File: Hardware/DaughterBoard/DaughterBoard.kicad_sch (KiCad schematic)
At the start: 13 parts, among them J1 CARTDRIGE, J2 ROM, J3 ISA00, J4 ISA10, J7 ISA01, J8 ISA11, SW1 RESET

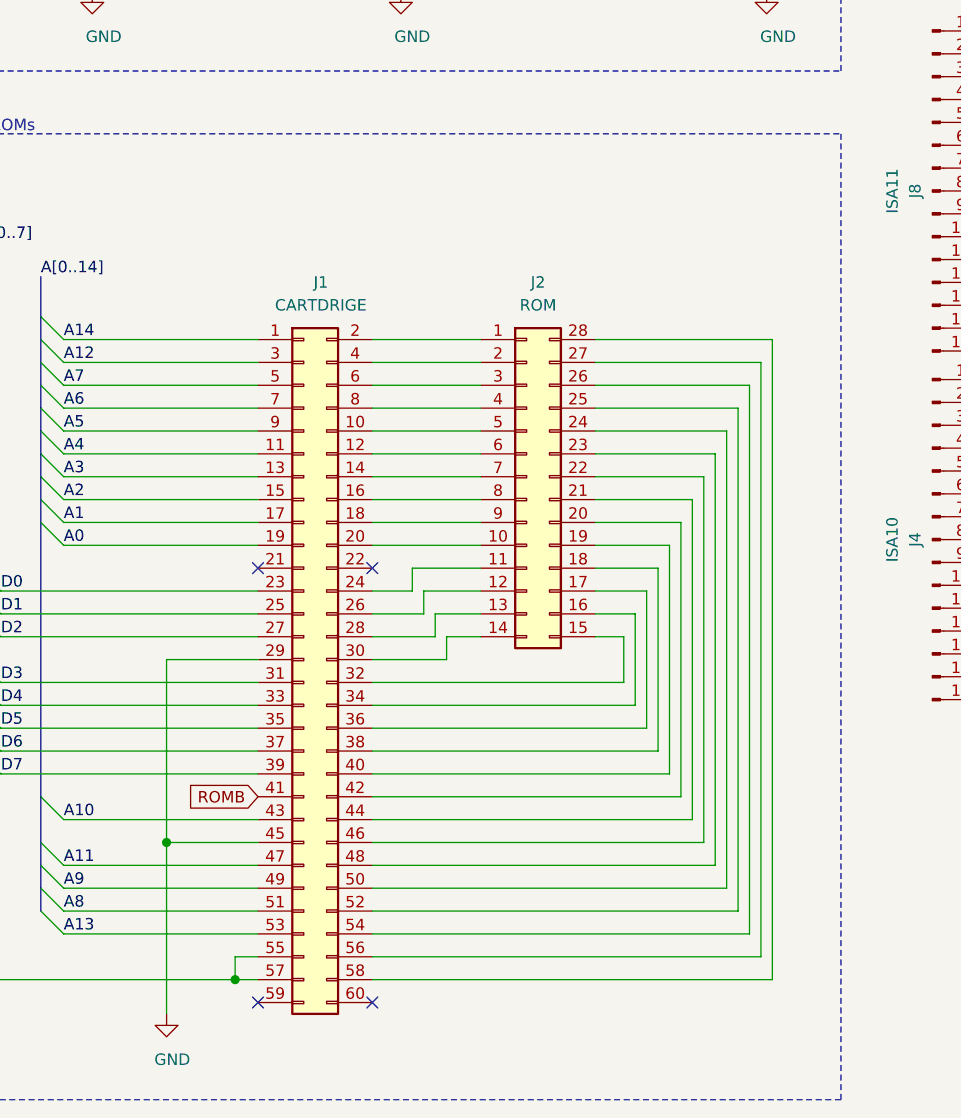
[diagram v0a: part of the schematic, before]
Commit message: implement graphic loading from ROM
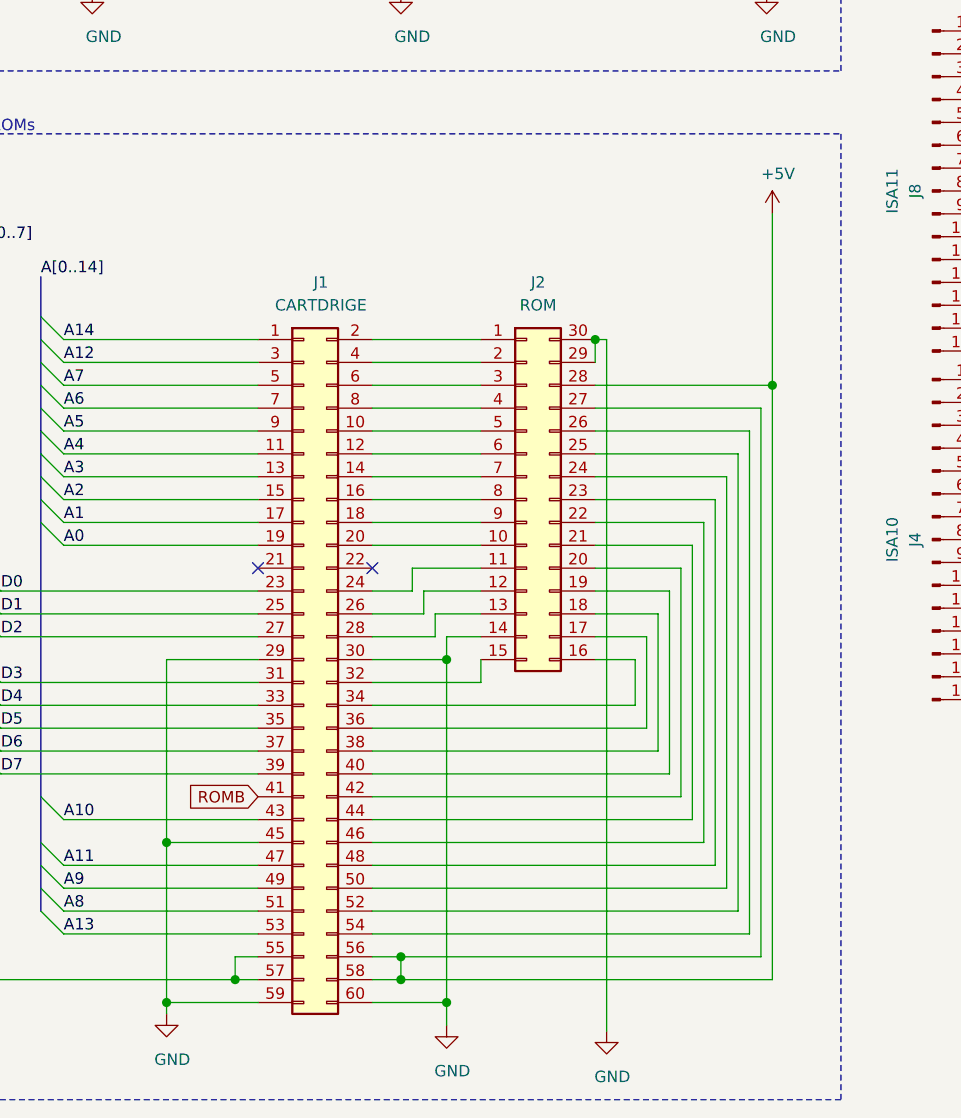
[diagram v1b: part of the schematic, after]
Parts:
- J1: footprint Connector_PCBEdge:Samtec_MECF-30-02-L-DV_2x30_P1.27mm_Polarized_Socket_Horizontal -> Connector_PCBEdge:Samtec_MECF-30-01-L-DV-WT_2x30_P1.27mm_Polarized_Socket_Horizontal
- J2: footprint Connector_PinHeader_2.54mm:PinHeader_2x14_P2.54mm_Vertical -> Connector_PinHeader_2.54mm:PinHeader_2x15_P2.54mm_Vertical; symbol Connector_Generic:Conn_02x14_Counter_Clockwise -> Connector_Generic:Conn_02x15_Counter_Clockwise
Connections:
- net +5V: now also J1.56 (Pin_56), J1.58 (Pin_58), J2.27 (Pin_27), J2.28 (Pin_28)
- net GND: now also J1.30 (Pin_30), J1.59 (Pin_59), J1.60 (Pin_60), J2.14 (Pin_14), J2.29 (Pin_29), J2.30 (Pin_30)
- no-connect marks 5 -> 3

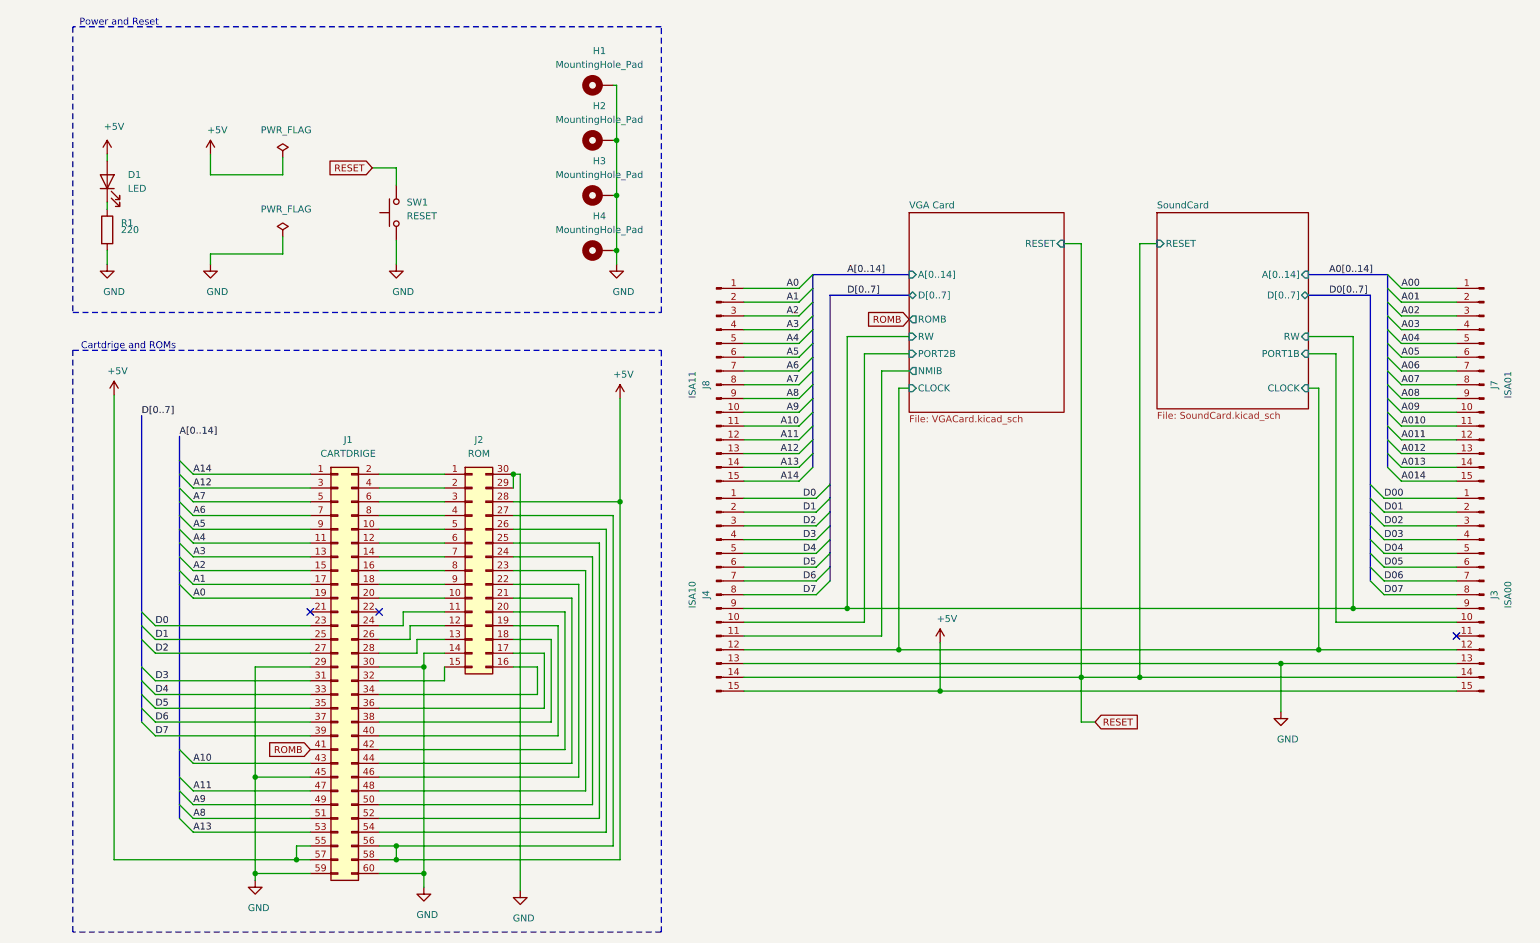
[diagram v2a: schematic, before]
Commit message: Implement APU and fix schematics
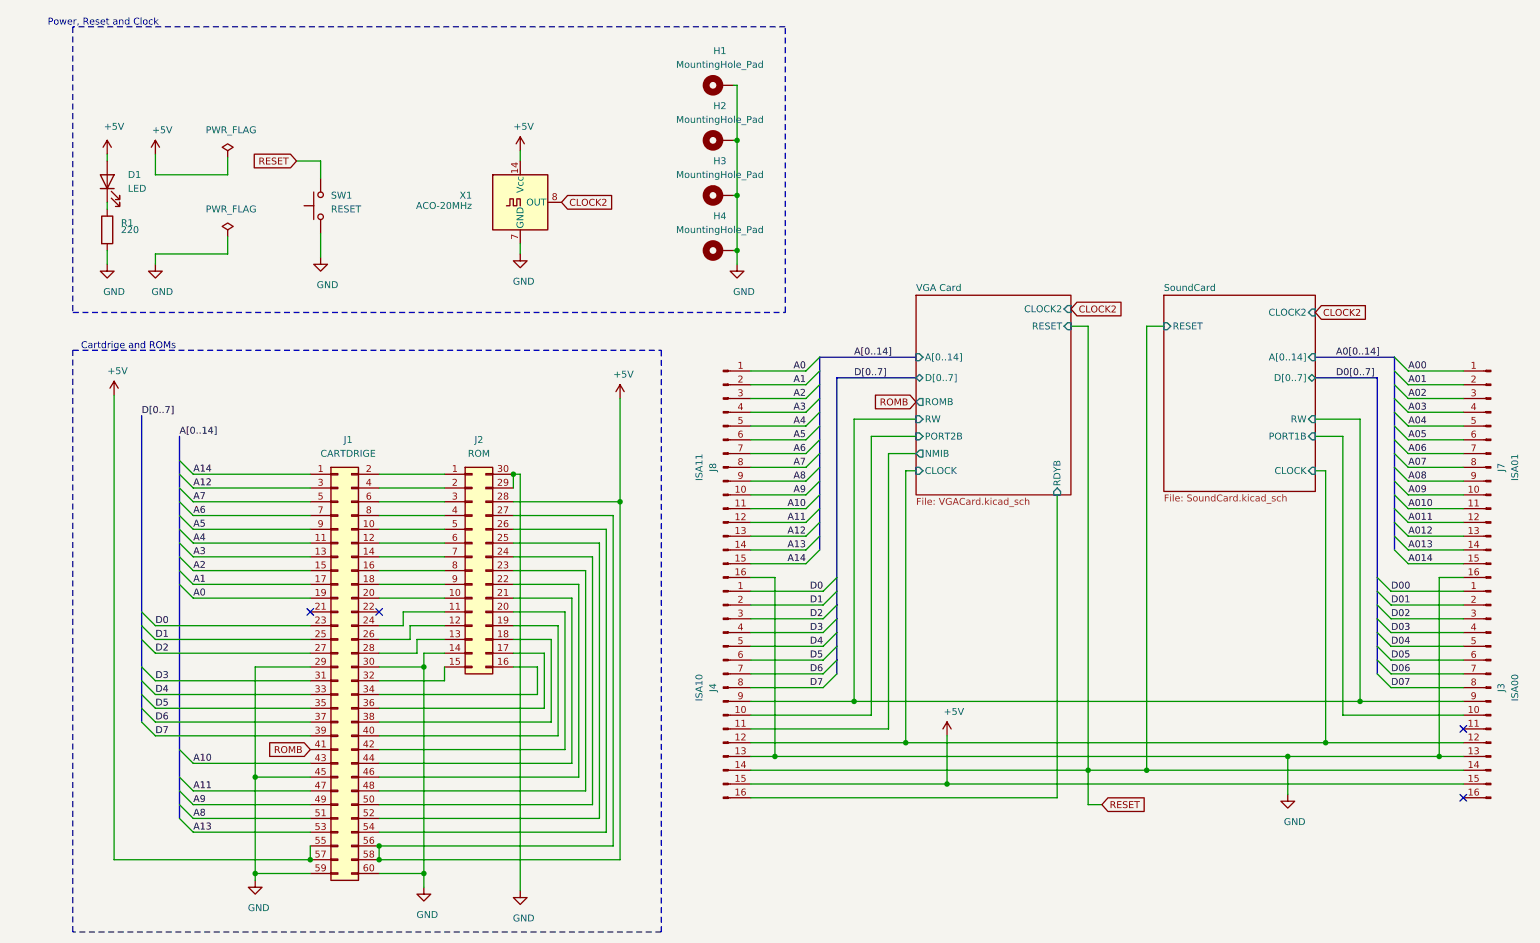
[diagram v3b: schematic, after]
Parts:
- added X1: ACO-20MHz, Oscillator:Oscillator_DIP-14, symbol Oscillator:ACO-xxxMHz
- J3, J4, J7, J8: footprint Connector_PinHeader_2.54mm:PinHeader_1x15_P2.54mm_Vertical -> Connector_PinHeader_2.54mm:PinHeader_1x16_P2.54mm_Vertical; symbol Connector:Conn_01x15_Male -> Connector:Conn_01x16_Male
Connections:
- net +5V: now also X1.14 (Vcc)
- net GND: now also J7.16 (Pin_16), J8.16 (Pin_16), X1.7 (GND)
- new net CLOCK2: X1.8 (OUT)
- new net VGA Card/RDYB: J4.16 (Pin_16)
- no-connect marks 3 -> 4
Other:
- sheet SoundCard ports: added CLOCK2; removed none
- sheet VGA Card ports: added CLOCK2, RDYB; removed none
- note added: "Power, Reset and Clock"
- note removed: "Power and Reset"
- moved on the sheet: H1, H2, H3, H4, SW1

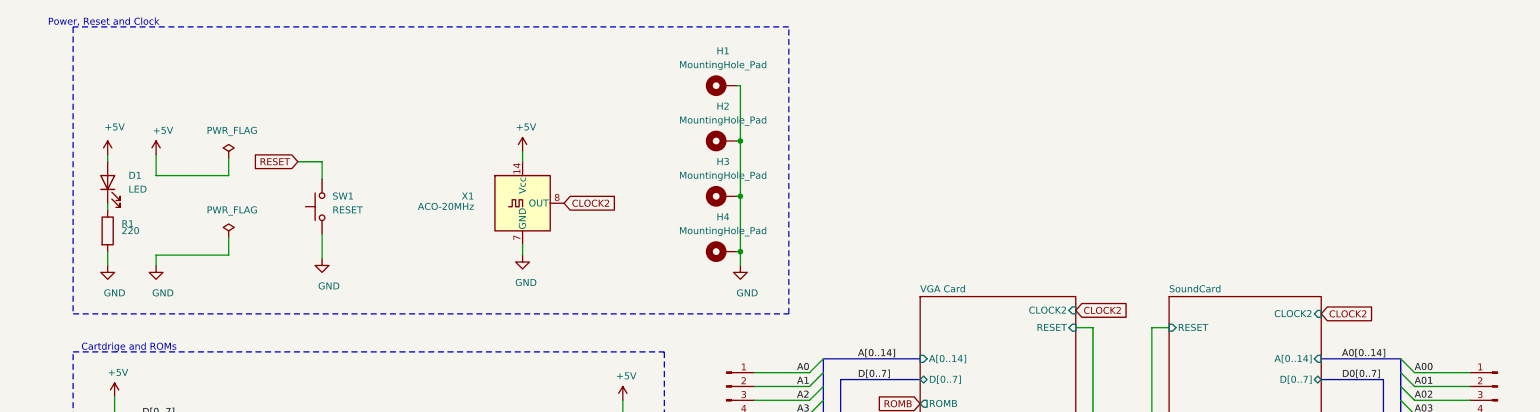
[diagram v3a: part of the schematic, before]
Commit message: Implement DMA and PCB ports
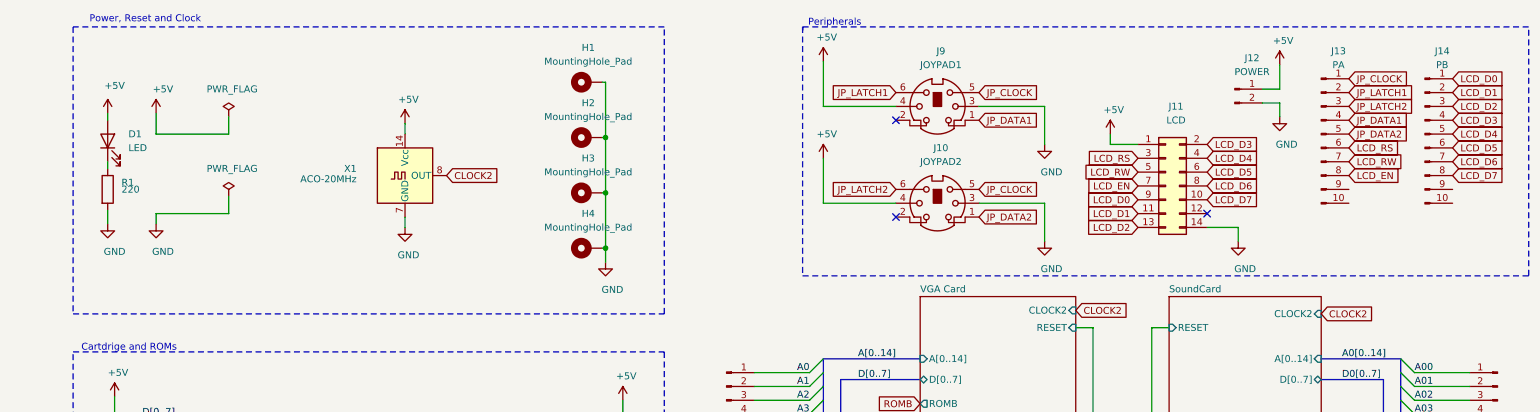
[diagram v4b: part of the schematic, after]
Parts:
- removed SW1: RESET, Button_Switch_THT:SW_PUSH_6mm_H5mm, symbol Switch:SW_Push
- added J10: JOYPAD2, Connector_PinSocket_2.54mm:PinSocket_2x04_P2.54mm_Vertical, symbol Connector:Mini-DIN-6
- added J11: LCD, Connector_PinHeader_2.54mm:PinHeader_2x07_P2.54mm_Vertical, symbol Connector_Generic:Conn_02x07_Odd_Even
- added J12: POWER, Connector_PinHeader_2.54mm:PinHeader_1x02_P2.54mm_Vertical, symbol Connector:Conn_01x02_Male
- added J13: PA, Connector_PinHeader_2.54mm:PinHeader_1x10_P2.54mm_Vertical, symbol Connector:Conn_01x10_Male
- added J14: PB, Connector_PinHeader_2.54mm:PinHeader_1x10_P2.54mm_Vertical, symbol Connector:Conn_01x10_Male
- added J9: JOYPAD1, Connector_PinSocket_2.54mm:PinSocket_2x04_P2.54mm_Vertical, symbol Connector:Mini-DIN-6
- J1: footprint Connector_PCBEdge:Samtec_MECF-30-01-L-DV-WT_2x30_P1.27mm_Polarized_Socket_Horizontal -> Connector_PinSocket_2.54mm:PinSocket_2x30_P2.54mm_Vertical
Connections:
- net +5V: now also J10.4, J11.1 (Pin_1), J12.1 (Pin_1), J9.4
- net GND: now also J10.3, J11.14 (Pin_14), J12.2 (Pin_2), J9.3
- new net JP_CLOCK: J10.5, J13.1 (Pin_1), J9.5
- new net JP_DATA1: J13.4 (Pin_4), J9.1
- new net JP_DATA2: J10.1, J13.5 (Pin_5)
- new net JP_LATCH1: J13.2 (Pin_2), J9.6
- new net JP_LATCH2: J10.6, J13.3 (Pin_3)
- new net LCD_D0: J11.9 (Pin_9), J14.1 (Pin_1)
- new net LCD_D1: J11.11 (Pin_11), J14.2 (Pin_2)
- new net LCD_D2: J11.13 (Pin_13), J14.3 (Pin_3)
- new net LCD_D3: J11.2 (Pin_2), J14.4 (Pin_4)
- new net LCD_D4: J11.4 (Pin_4), J14.5 (Pin_5)
- new net LCD_D5: J11.6 (Pin_6), J14.6 (Pin_6)
- new net LCD_D6: J11.8 (Pin_8), J14.7 (Pin_7)
- new net LCD_D7: J11.10 (Pin_10), J14.8 (Pin_8)
- new net LCD_EN: J11.7 (Pin_7), J13.8 (Pin_8)
- new net LCD_RS: J11.3 (Pin_3), J13.6 (Pin_6)
- new net LCD_RW: J11.5 (Pin_5), J13.7 (Pin_7)
- no-connect marks 4 -> 7
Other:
- note added: "Peripherals"
- moved on the sheet: D1, H1, H2, H3, H4, R1, X1

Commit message: Version 1.2
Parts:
- removed J10: JOYPAD2, Connector_PinSocket_2.54mm:PinSocket_2x04_P2.54mm_Vertical, symbol Connector:Mini-DIN-6
- removed J9: JOYPAD1, Connector_PinSocket_2.54mm:PinSocket_2x04_P2.54mm_Vertical, symbol Connector:Mini-DIN-6
- added J10: JOYPAD2, Connector_TheRLab:NES_JoyPad, symbol Connector_TheRLab:NES_JoyPad
- added J9: JOYPAD1, Connector_TheRLab:NES_JoyPad, symbol Connector_TheRLab:NES_JoyPad
- J1: footprint Connector_PinSocket_2.54mm:PinSocket_2x30_P2.54mm_Vertical -> Connector_PinHeader_2.54mm:PinHeader_2x15_P2.54mm_Vertical; symbol Connector_Generic:Conn_02x30_Odd_Even -> Connector_Generic:Conn_02x15_Counter_Clockwise
- J11: footprint Connector_PinHeader_2.54mm:PinHeader_2x07_P2.54mm_Vertical -> Connector_IDC:IDC-Header_2x10_P2.54mm_Vertical; symbol Connector_Generic:Conn_02x07_Odd_Even -> Connector_Generic:Conn_02x10_Odd_Even
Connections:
- net +5V: now also J1.27 (Pin_27), J1.28 (Pin_28), J3.16 (Pin_16), J4.16 (Pin_16), J10.7 (VCC), J9.7 (VCC); no longer J1.55 (Pin_55), J1.56 (Pin_56), J1.57 (Pin_57), J1.58 (Pin_58), J3.15 (Pin_15), J4.15 (Pin_15)
- net A0: no longer J1.19 (Pin_19)
- net A1: no longer J1.17 (Pin_17)
- net A10: no longer J1.43 (Pin_43)
- net A11: no longer J1.47 (Pin_47)
- net A12: no longer J1.3 (Pin_3)
- net A13: no longer J1.53 (Pin_53)
- net A14: no longer J1.1 (Pin_1)
- net A2: no longer J1.15 (Pin_15)
- net A3: no longer J1.13 (Pin_13)
- net A4: no longer J1.11 (Pin_11)
- net A5: no longer J1.9 (Pin_9)
- net A6: no longer J1.7 (Pin_7)
- net A7: no longer J1.5 (Pin_5)
- net A8: no longer J1.51 (Pin_51)
- net A9: no longer J1.49 (Pin_49)
- net D0: no longer J1.23 (Pin_23)
- net D1: no longer J1.25 (Pin_25)
- net D2: no longer J1.27 (Pin_27)
- net D3: no longer J1.31 (Pin_31)
- net D4: no longer J1.33 (Pin_33)
- net D5: no longer J1.35 (Pin_35)
- net D6: no longer J1.37 (Pin_37)
- net D7: no longer J1.39 (Pin_39)
- net GND: now also J1.14 (Pin_14), J11.18 (Pin_18), J11.20 (Pin_20), J3.15 (Pin_15), J10.1 (GND), J9.1 (GND); no longer J1.45 (Pin_45), J1.59 (Pin_59), J1.60 (Pin_60), J11.14 (Pin_14), J7.16 (Pin_16)
- net JP_CLOCK: now also J10.2 (CLOCK), J9.2 (CLOCK)
- net JP_DATA1: now also J9.4 (D1)
- net JP_DATA2: now also J10.4 (D1)
- net JP_LATCH1: now also J9.3 (LATCH)
- net JP_LATCH2: now also J10.3 (LATCH)
- net LCD_D3: now also J11.6 (Pin_6); no longer J11.2 (Pin_2)
- net LCD_D4: now also J11.8 (Pin_8); no longer J11.4 (Pin_4)
- net LCD_D5: now also J11.10 (Pin_10); no longer J11.6 (Pin_6)
- net LCD_D6: now also J11.12 (Pin_12); no longer J11.8 (Pin_8)
- net LCD_D7: now also J11.14 (Pin_14); no longer J11.10 (Pin_10)
- net VGA Card/RDYB: now also J4.15 (Pin_15); no longer J4.16 (Pin_16)
- net at J2.1 (Pin_1): now also J1.1 (Pin_1); no longer J1.2 (Pin_2)
- net at J2.10 (Pin_10): now also J1.10 (Pin_10); no longer J1.20 (Pin_20)
- net at J2.11 (Pin_11): now also J1.11 (Pin_11); no longer J1.24 (Pin_24)
- net at J2.12 (Pin_12): now also J1.12 (Pin_12); no longer J1.26 (Pin_26)
- net at J2.13 (Pin_13): now also J1.13 (Pin_13); no longer J1.28 (Pin_28)
- net at J2.15 (Pin_15): now also J1.15 (Pin_15); no longer J1.32 (Pin_32)
- net at J2.16 (Pin_16): now also J1.16 (Pin_16); no longer J1.34 (Pin_34)
- net at J2.17 (Pin_17): now also J1.17 (Pin_17); no longer J1.36 (Pin_36)
- net at J2.18 (Pin_18): now also J1.18 (Pin_18); no longer J1.38 (Pin_38)
- net at J2.19 (Pin_19): now also J1.19 (Pin_19); no longer J1.40 (Pin_40)
- net at J2.2 (Pin_2): now also J1.2 (Pin_2); no longer J1.4 (Pin_4)
- net at J2.20 (Pin_20): now also J1.20 (Pin_20); no longer J1.42 (Pin_42)
- net at J2.21 (Pin_21): now also J1.21 (Pin_21); no longer J1.44 (Pin_44)
- net at J2.22 (Pin_22): now also J1.22 (Pin_22); no longer J1.46 (Pin_46)
- net at J2.23 (Pin_23): now also J1.23 (Pin_23); no longer J1.48 (Pin_48)
- net at J2.24 (Pin_24): now also J1.24 (Pin_24); no longer J1.50 (Pin_50)
- net at J2.25 (Pin_25): now also J1.25 (Pin_25); no longer J1.52 (Pin_52)
- net at J2.26 (Pin_26): now also J1.26 (Pin_26); no longer J1.54 (Pin_54)
- net at J2.3 (Pin_3): now also J1.3 (Pin_3); no longer J1.6 (Pin_6)
- net at J2.4 (Pin_4): now also J1.4 (Pin_4); no longer J1.8 (Pin_8)
- net at J2.5 (Pin_5): now also J1.5 (Pin_5); no longer J1.10 (Pin_10)
- net at J2.6 (Pin_6): now also J1.6 (Pin_6); no longer J1.12 (Pin_12)
- net at J2.7 (Pin_7): now also J1.7 (Pin_7); no longer J1.14 (Pin_14)
- net at J2.8 (Pin_8): now also J1.8 (Pin_8); no longer J1.16 (Pin_16)
- net at J2.9 (Pin_9): now also J1.9 (Pin_9); no longer J1.18 (Pin_18)
- net SoundCard/IRQ0B: now reaches J3.11 (Pin_11)
- net CA2: now reaches J13.10 (Pin_10)
- net CA2: now also J11.17 (Pin_17)
- net CA1: now reaches J13.9 (Pin_9)
- net CA1: now also J11.15 (Pin_15)
- net CB2: now reaches J14.10 (Pin_10)
- net CB2: now also J11.4 (Pin_4)
- net CB1: now reaches J14.9 (Pin_9)
- net CB1: now also J11.2 (Pin_2)
- removed net ROMB: J1.41 (Pin_41)
- new net A015: J7.16 (Pin_16)
- no-connect marks 7 -> 6
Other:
- sheet SoundCard ports: added A[0..15], IRQ0B; removed A[0..14]
- sheet VGA Card ports: added A[0..15]; removed A[0..14], ROMB
- moved on the sheet: J12, J13, J14, J2, J3, J4, J7, J8
